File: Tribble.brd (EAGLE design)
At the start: 154.5 x 47.2 mm, 106 parts, among them J1 10118193-0001LF, J2 68602-406HLF, J3 SJ1-2503A, J4 RJHSE-5381, J5 SJ1-2503A, J6 SJ1-2503A, J7 HFW6R-2STE1LF, P1 TC33X-2, U1 AT90USB646-MU, U10 IP4234CZ6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

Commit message: fixed minor issues with REV6.
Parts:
- moved J3 0.80 mm to (30.8, 18.3)
- moved J5 0.80 mm to (-36.5, 18.3)
- moved J6 0.80 mm to (10.5, 18.3)
- moved J1 0.50 mm to (20.8, 15.5)
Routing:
- net +5V: track 526.5 -> 529.9 mm
- net OK_SHT: track 63.9 -> 62.3 mm
- net IO_2: track 49.2 -> 50.8 mm
- net IO_3: track 55.5 -> 57.0 mm
- net UGND: track 68.7 -> 69.5 mm
- net IO_1: track 52.9 -> 52.1 mm
- net CAM_COM: track 27.9 -> 28.6 mm
- net MOSI: track 60.7 -> 60.1 mm
- net CAM_SHT: track 11.5 -> 12.1 mm
- net D-: track 5.13 -> 5.63 mm
- net D+: track 5.19 -> 5.69 mm
- net VIN: vias 24 -> 22

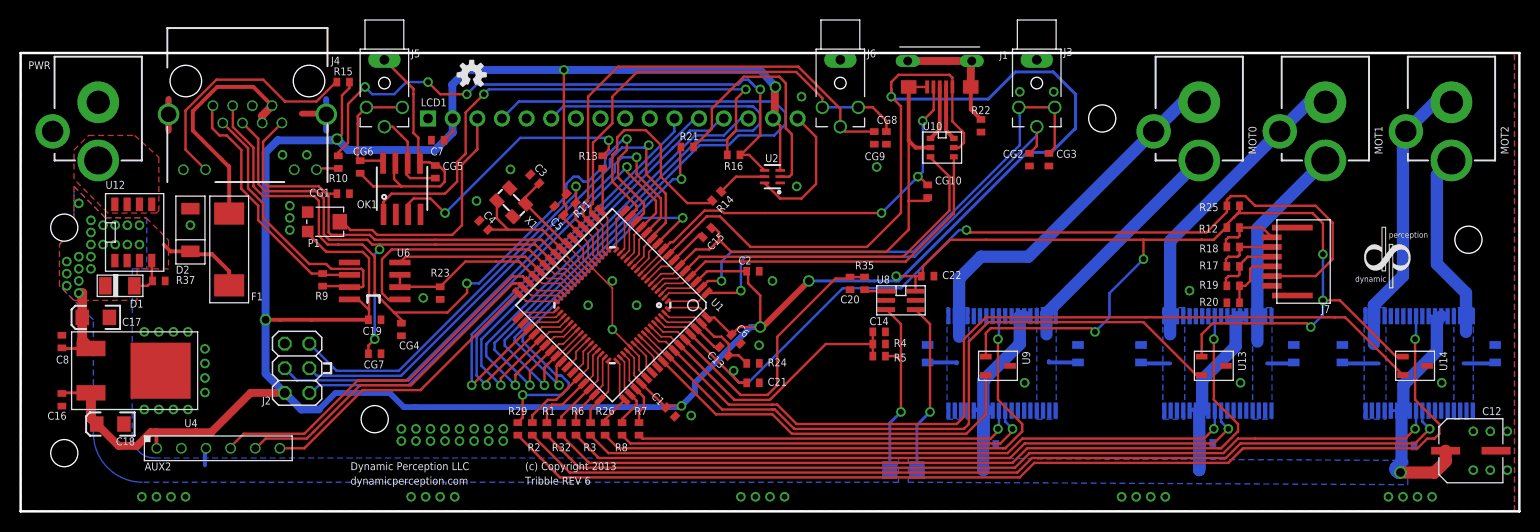
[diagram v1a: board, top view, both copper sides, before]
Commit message: Fixing EMC problems with Tribble. Moved lots of traces. Added Ferrite beads to COM1, COM2, Com3. Added proper support for USB OTG
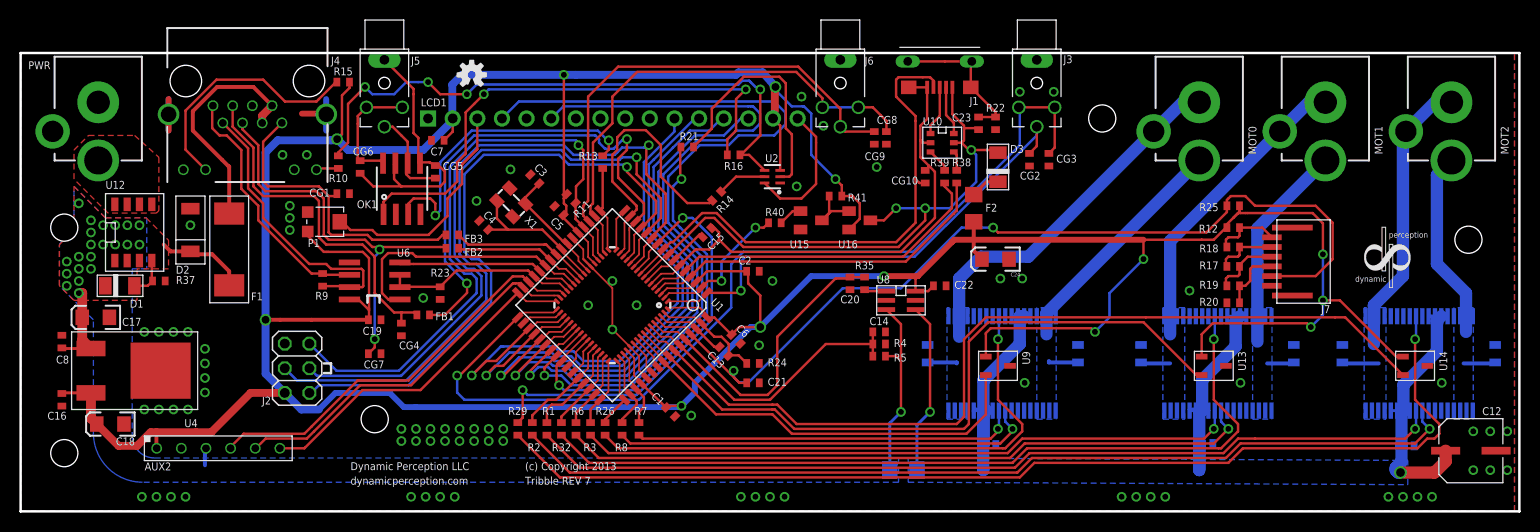
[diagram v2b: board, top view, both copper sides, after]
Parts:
- added C23: .1uF, parkers_parts:0402_CAP
- added C24: 10uF, SparkFun:EIA3216
- added D3: PMEG3010BER,115, PP_Passives:SOD-123
- added F2: 1206L025YR, PP_Passives:1206
- added FB1, FB2, FB3: LI0402C470R-10, parkers_parts:0402_RES
- added R38, R39: 22, parkers_parts:0402_RES
- added R40: 100K, parkers_parts:0402_RES
- added R41: 10K, parkers_parts:0402_RES
- added U15: BC847BMTF, PP_DiscreteSemi:SOT-23
- added U16: FDV304P, PP_DiscreteSemi:SOT-23
- J1: device SparkFun-Connectors:-PTH-MICROB -> PP_Connectors:10118193-0001LF
- U10: device parkers_parts:SOT-457 -> PP_Passives:SOT-457
- moved J1 2.50 mm to (20.8, 18.0)
- moved C22 1.60 mm to (20.8, -5.00)
- moved CG10 1.52 mm to (19.2, 6.25), turned to 270 degrees
- moved R22 1.52 mm to (26.5, 11.8)
- moved U10 0.50 mm to (21.0, 9.75)
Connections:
- removed net PE0: U1.33, U11.33
- new net COM1_FB: CG4.1, FB1.1, J4.3
- new net COM2_FB: CG7.1, FB2.1, J4.4
- new net COM3_FB: CG1.2, FB3.1, J4.8
- new net FDV_GATE: R41.2, U15.3, U16.1
- new net N$11: R38.1, U10.4
- new net N$13: R39.1, U10.3
- new net N$14: D3.1, F2.1
- new net PE7: R40.2, U1.2, U11.2
- new net PE7_GATE: R40.1, U15.1
- new net V_USB: C23.2, D3.2, J1.1, U1.8, U10.5, U11.8, U16.3
- net +5V: now also C24.A, F2.2, R41.1, U16.2; no longer J1.1, U1.8, U10.5, U11.8
- net COM1: now also FB1.2; no longer CG4.1, J4.3
- net COM2: now also FB2.2; no longer CG7.1, J4.4
- net COM3: now also FB3.2; no longer CG1.2, J4.8
- net GND: now also C24.C, U15.2
- net IO_3: now also U1.33, U11.33; no longer U1.2, U11.2
- net PE3: now also J1.4
- net RD+: now also R39.2; no longer U10.3
- net RD-: now also R38.2; no longer U10.4
- net UGND: now also C23.1, CG10.1
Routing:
- net +5V: track 529.9 -> 436.8 mm, vias 14 -> 13
- net V_USB: track 0.00 -> 64.2 mm, vias 0 -> 3
- net COM2: track 57.9 -> 13.7 mm, vias 2 -> 0
- net COM2_FB: track 0.00 -> 42.8 mm, vias 0 -> 2
- net IO_3: track 57.0 -> 99.3 mm
- net COM1_FB: track 0.00 -> 37.0 mm
- net COM3: track 47.7 -> 14.5 mm
- net COM3_FB: track 0.00 -> 31.5 mm
- net COM1: track 82.9 -> 54.7 mm
- net RST: track 45.5 -> 64.7 mm
- net PE3: track 36.2 -> 55.2 mm, vias 2 -> 0
- net PE7: track 0.00 -> 15.2 mm, vias 0 -> 2
- net MISO: track 54.5 -> 67.7 mm
- net MOSI: track 60.1 -> 72.6 mm
- net SCK: track 60.5 -> 72.8 mm
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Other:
- board text added: "Tribble REV 7"
- board text removed: "Tribble REV 6"
